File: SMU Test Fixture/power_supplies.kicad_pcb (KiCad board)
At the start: 2 copper layers, 84.9 x 130.1 mm, 47 parts, among them J13 Hot_Spade, J14 Power Outputs, J15 Neutral_Spade, Q1 IRFL014, Q2 IRFL014, T1 VPP28-1060, U10 LT3045, U11 LT1086-12, U12 LT3094, U9 LT1086-5.0

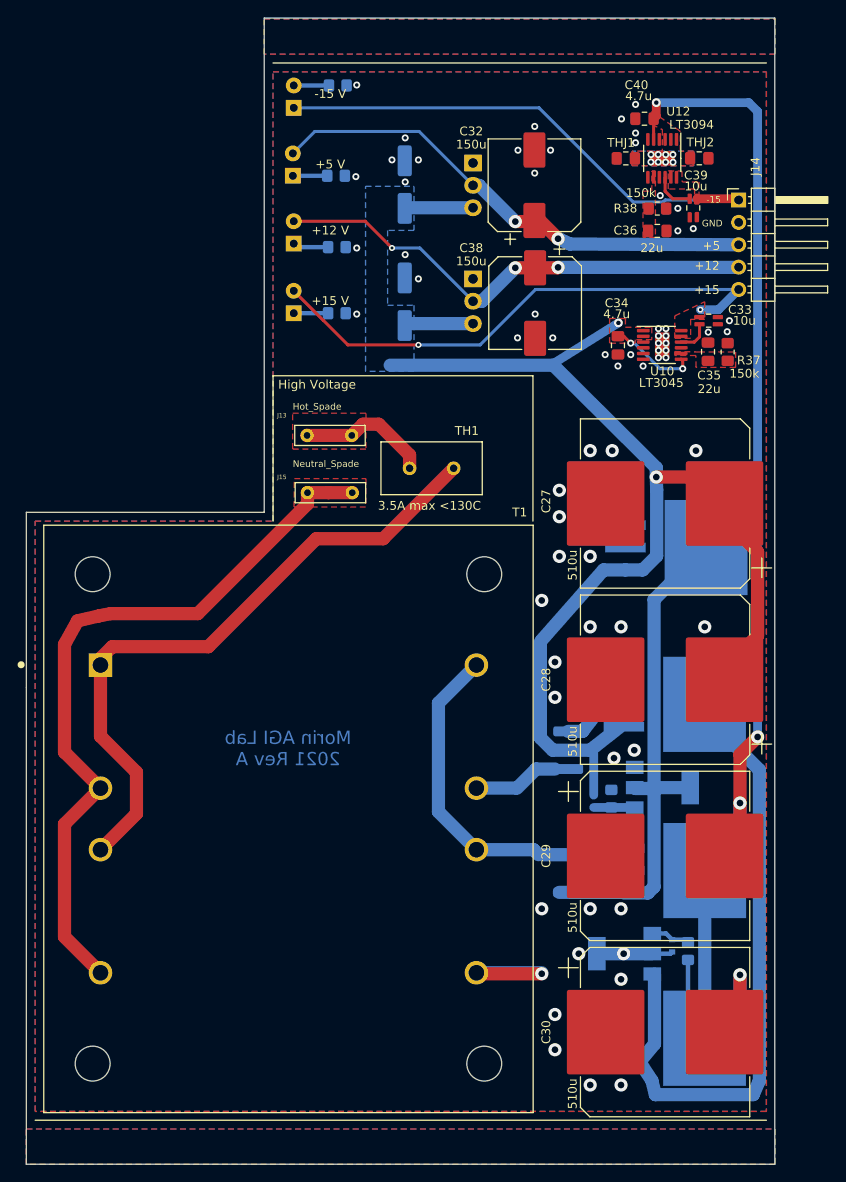
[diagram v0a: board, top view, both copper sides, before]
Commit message: Daisy-chain 12V->5V regs.
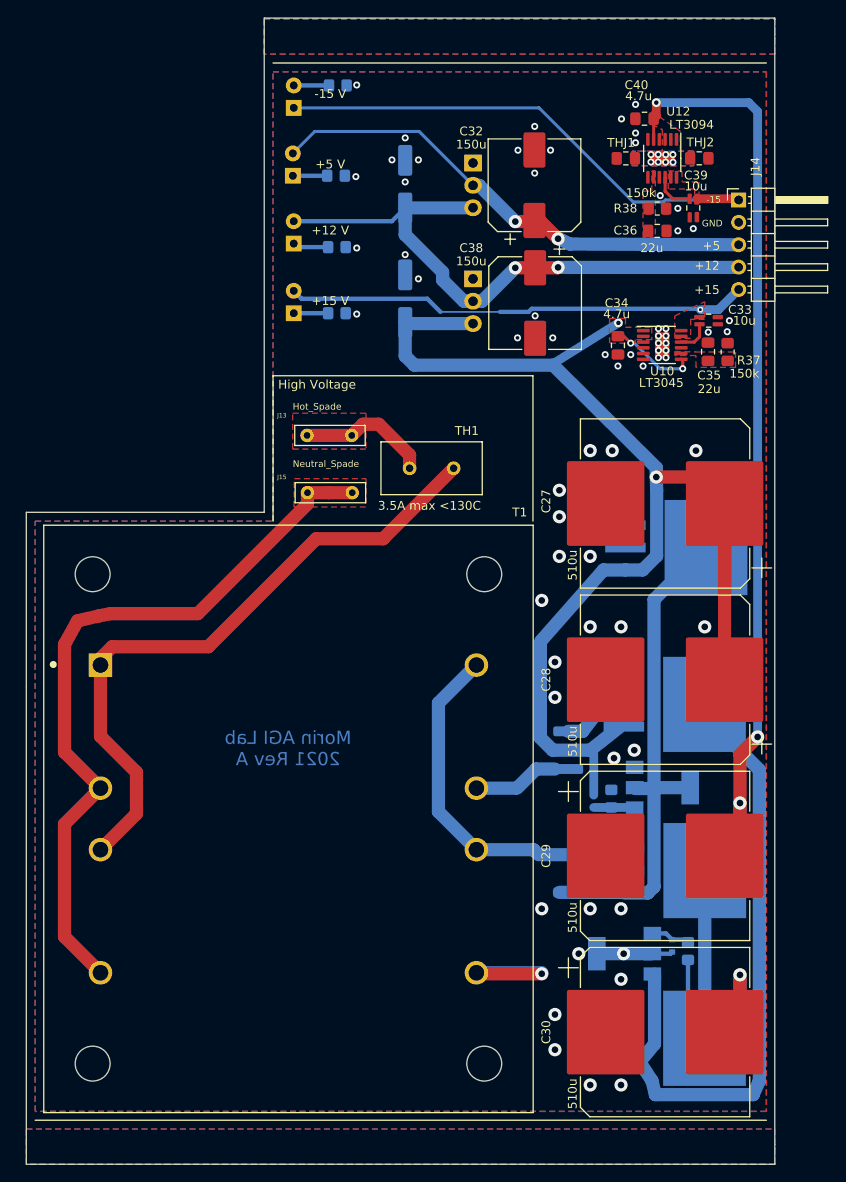
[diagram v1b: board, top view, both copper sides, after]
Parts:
- moved C31 13.4 mm to (147.0, 47.8)
- moved C37 13.0 mm to (147.0, 60.8)
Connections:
- C31 pad 1: /unreg_pos_18VDC -> +12V
- U9 pad 3: /unreg_pos_18VDC -> +12V
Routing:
- net /unreg_pos_18VDC: track 162.5 -> 151.2 mm
- net +12V: track 55.9 -> 67.1 mm, vias 3 -> 2
- net +15V: track 64.7 -> 56.4 mm, vias 2 -> 1
- removed copper zone on B.Cu, net /unreg_pos_18VDC
